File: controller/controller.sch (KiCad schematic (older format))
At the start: 5 parts

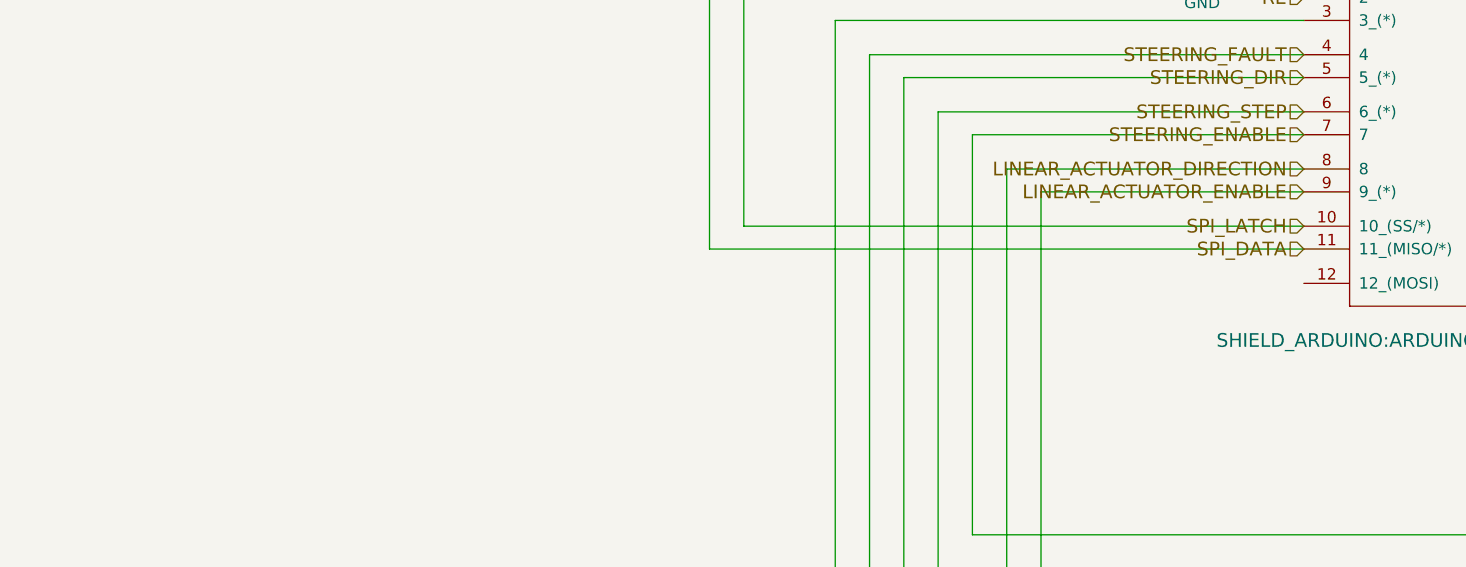
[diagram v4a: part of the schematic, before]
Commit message: send controller and line interface boards for manufacturing
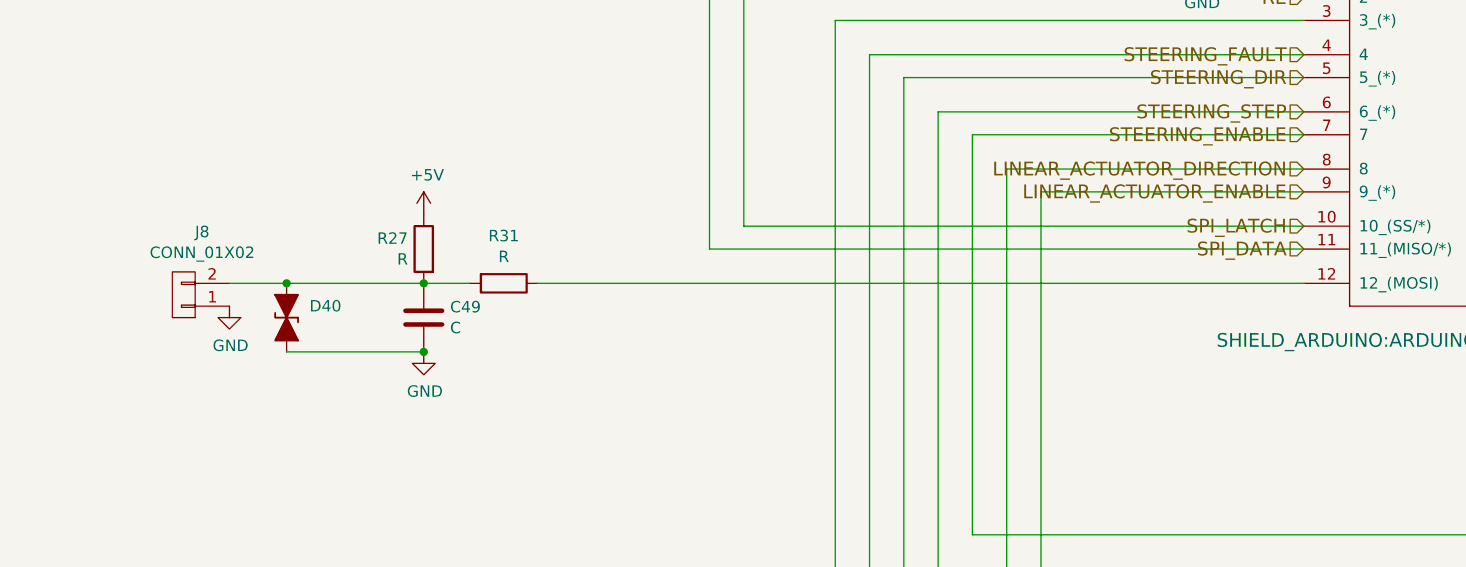
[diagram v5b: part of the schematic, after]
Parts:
- added C49: C, Capacitors_SMD:C_0603_HandSoldering, symbol C
- added D40: D_TVS_ALT, Diodes_SMD:SOD-323, symbol D_TVS_ALT
- added J8: CONN_01X02, Connectors_JST:JST_EH_B02B-EH-A_02x2.50mm_Straight, symbol CONN_01X02
- added R27, R31: R, Resistors_SMD:R_0603_HandSoldering, symbol R
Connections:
- net GND: now also C49.2, D40.2 (A2), J8.1 (P1)
- net at SH1.12 (12_(MOSI)): now also R31.1
- new net: C49.1, D40.1 (A1), J8.2 (P2), R27.2, R31.2
- new net +5V: R27.1
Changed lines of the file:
@@
 LINEAR_ACTUATOR_DIRECTION
 $Comp
-L GND #PWR01
+L GND #PWR5
 U 1 1 58CADA03
 P 8050 9050
-F 0 "#PWR01" H 8050 8800 50  0001 C CNN
+F 0 "#PWR5" H 8050 8800 50  0001 C CNN
 F 1 "GND" H 8055 8877 50  0000 C CNN
 F 2 "" H 8050 9050 50  0001 C CNN
@@
 $EndComp
 $Comp
-L GND #PWR02
+L GND #PWR4
 U 1 1 58CAF659
 P 6100 9300
-F 0 "#PWR02" H 6100 9050 50  0001 C CNN
+F 0 "#PWR4" H 6100 9050 50  0001 C CNN
 F 1 "GND" H 6105 9127 50  0000 C CNN
 F 2 "" H 6100 9300 50  0001 C CNN
@@
 Connection ~ 13050 2650
 Connection ~ 8600 2650
+Wire Wire Line
+	6550 10700 3200 10700
+$Comp
+L R R31
+U 1 1 58D00753
+P 3050 10700
+F 0 "R31" V 2843 10700 50  0000 C CNN
+F 1 "R" V 2934 10700 50  0000 C CNN
+F 2 "Resistors_SMD:R_0603_HandSoldering" V 2980 10700 50  0001 C CNN
+F 3 "" H 3050 10700 50  0001 C CNN
+F 4 "?" H 3050 10700 60  0001 C CNN "PartNo"
+F 5 "?" H 3050 10700 60  0001 C CNN "Manufacturer"
+F 6 "?" H 3050 10700 60  0001 C CNN "Distributor"
+	1    3050 10700
+	0    1    1    0
+$EndComp
+$Comp
+L CONN_01X02 J8
+U 1 1 58D042B0
+P 1650 10750
+F 0 "J8" H 1569 10475 50  0000 C CNN
+F 1 "CONN_01X02" H 1569 10566 50  0000 C CNN
+F 2 "Connectors_JST:JST_EH_B02B-EH-A_02x2.50mm_Straight" H 1650 10750 50  0001 C CNN
+F 3 "" H 1650 10750 50  0001 C CNN
+F 4 "?" H 1650 10750 60  0001 C CNN "PartNo"
+F 5 "?" H 1650 10750 60  0001 C CNN "Manufacturer"
+F 6 "?" H 1650 10750 60  0001 C CNN "Distributor"
+	1    1650 10750
+	-1   0    0    1
+$EndComp
+$Comp
+L GND #PWR1
+U 1 1 58D051F0
+P 1850 10800
+F 0 "#PWR1" H 1850 10550 50  0001 C CNN
+F 1 "GND" H 1855 10627 50  0000 C CNN
+F 2 "" H 1850 10800 50  0001 C CNN
+F 3 "" H 1850 10800 50  0001 C CNN
+	1    1850 10800
+	1    0    0    -1
+$EndComp
+Wire Wire Line
+	1850 10700 2900 10700
+$Comp
+L C C49
+U 1 1 58D06091
+P 2700 10850
+F 0 "C49" H 2815 10896 50  0000 L CNN
+F 1 "C" H 2815 10805 50  0000 L CNN
+F 2 "Capacitors_SMD:C_0603_HandSoldering" H 2738 10700 50  0001 C CNN
+F 3 "" H 2700 10850 50  0001 C CNN
+F 4 "?" H 2700 10850 60  0001 C CNN "PartNo"
+F 5 "?" H 2700 10850 60  0001 C CNN "Manufacturer"
+F 6 "?" H 2700 10850 60  0001 C CNN "Distributor"
+	1    2700 10850
+	1    0    0    -1
+$EndComp
+Connection ~ 2700 10700
+$Comp
+L GND #PWR3
+U 1 1 58D065E2
+P 2700 11000
+F 0 "#PWR3" H 2700 10750 50  0001 C CNN
+F 1 "GND" H 2705 10827 50  0000 C CNN
+F 2 "" H 2700 11000 50  0001 C CNN
+F 3 "" H 2700 11000 50  0001 C CNN
+	1    2700 11000
+	1    0    0    -1
+$EndComp
+$Comp
+L R R27
+U 1 1 58D09756
+P 2700 10550
+F 0 "R27" H 2769 10596 50  0000 L CNN
+F 1 "R" H 2769 10505 50  0000 L CNN
+F 2 "Resistors_SMD:R_0603_HandSoldering" V 2630 10550 50  0001 C CNN
+F 3 "" H 2700 10550 50  0001 C CNN
+F 4 "?" H 2700 10550 60  0001 C CNN "PartNo"
+F 5 "?" H 2700 10550 60  0001 C CNN "Manufacturer"
+F 6 "?" H 2700 10550 60  0001 C CNN "Distributor"
+	1    2700 10550
+	-1   0    0    -1
+$EndComp
+$Comp
+L +5V #PWR2
+U 1 1 58D09F52
+P 2700 10400
+F 0 "#PWR2" H 2700 10250 50  0001 C CNN
+F 1 "+5V" H 2715 10573 50  0000 C CNN
+F 2 "" H 2700 10400 50  0001 C CNN
+F 3 "" H 2700 10400 50  0001 C CNN
+	1    2700 10400
+	1    0    0    -1
+$EndComp
+$Comp
+L D_TVS_ALT D40
+U 1 1 58D0C298
+P 2100 10850
+F 0 "D40" V 2050 10950 50  0000 L CNN
+F 1 "D_TVS_ALT" V 2145 10929 50  0001 L CNN
+F 2 "Diodes_SMD:SOD-323" H 2100 10850 50  0001 C CNN
+F 3 "" H 2100 10850 50  0001 C CNN
+F 4 "?" H 2100 10850 60  0001 C CNN "PartNo"
+F 5 "?" H 2100 10850 60  0001 C CNN "Manufacturer"
+F 6 "2059012" H 2100 10850 60  0001 C CNN "Distributor"
+	1    2100 10850
+	0    1    1    0
+$EndComp
+Connection ~ 2100 10700
+Wire Wire Line
+	2100 11000 2700 11000
+Connection ~ 2700 11000
 $EndSCHEMATC

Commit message: Last comments on the schematics
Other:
- note added: "FIX: 4 pin connector was used. sensors are powered from +5V_DIRTY as they consume 150mA each."
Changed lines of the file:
@@
 	2100 11000 2700 11000
 Connection ~ 2700 11000
+Text Notes -1000 11450 0    60   ~ 0
+FIX: 4 pin connector was used. sensors are powered from +5V_DIRTY as they consume 150mA each.
 $EndSCHEMATC
